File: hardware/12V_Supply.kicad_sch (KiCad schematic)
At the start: 26 parts, among them J4001 353180620, J4002 353180620, J4004 353180620

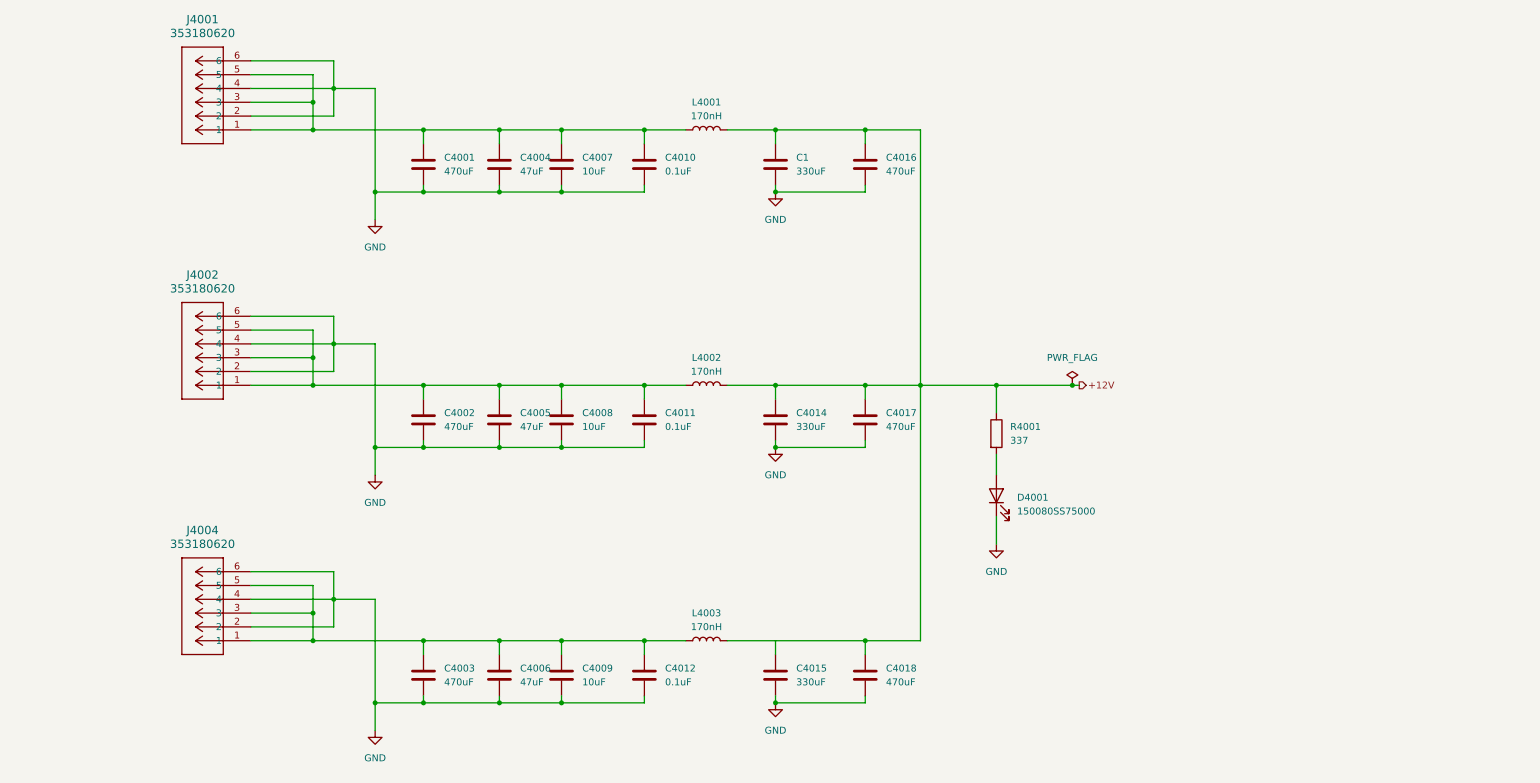
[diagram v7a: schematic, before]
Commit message: feat: fix pcb changes for 12V and low current supply
Swapped 5V regulator, added diodes, fixed connectors and general
placement. Changes to complete list for 12V and low current supply.
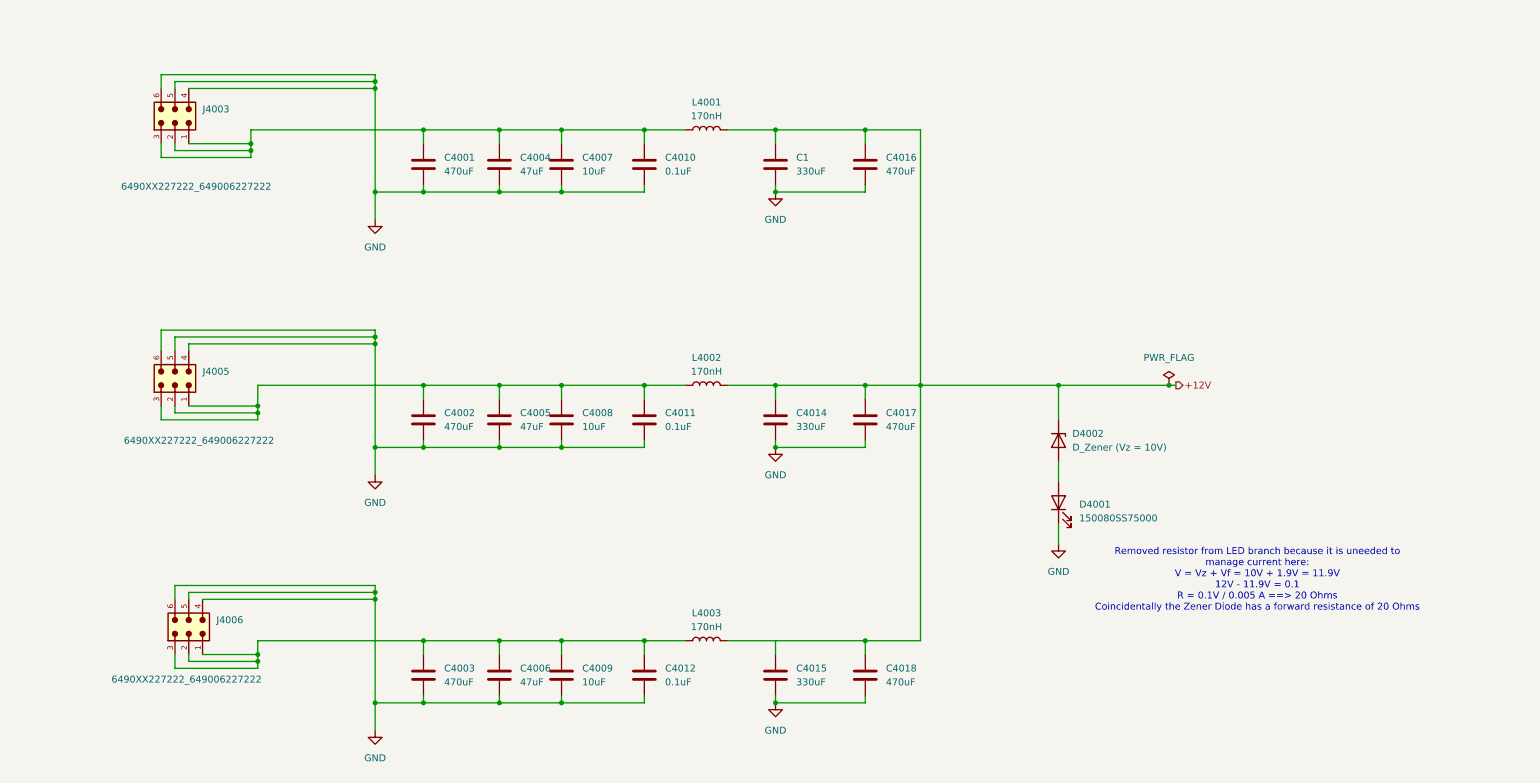
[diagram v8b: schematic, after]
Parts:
- removed J4001, J4002, J4004: 353180620, work:CONN_55690007-SD_06_MOL, symbol PCIe 2x3 Conn GPU:353180620
- removed R4001: 337, Resistor_SMD:R_0805_2012Metric, symbol Device:R
- added D4002: D_Zener (Vz = 10V), work:SOD123_DIO, symbol Device:D_Zener
- added J4003, J4005, J4006: 6490XX227222_649006227222, work:PCIe_2x3_Conn_Header, symbol PCIe 2x3 Header:6490XX227222_649006227222
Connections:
- net +12V: now also D4002.1 (K)
- net GND: now also J4003.4, J4003.5, J4003.6, J4005.4, J4005.5, J4005.6, J4006.4, J4006.5, J4006.6
- net at C4003.1, C4006.1, C4009.1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: now also J4006.1, J4006.2, J4006.3
- net at C4002.1, C4005.1, C4008.1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: now also J4005.1, J4005.2, J4005.3
- net at C4001.1, C4004.1, C4007.1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: now also J4003.1, J4003.2, J4003.3
- net at D4001.2 (A): now also D4002.2 (A)
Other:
- note added: "Removed resistor from LED branch because it is uneeded to manage current here: V = Vz + Vf = 10V + 1.9V = 11.9V 12V - 11.9V = 0.1 R = 0.1V / 0.005 A ==> 20 Ohms Coincidentally the Zener Diode has a forward resistance of 20 Ohms"
- moved on the sheet: D4001
